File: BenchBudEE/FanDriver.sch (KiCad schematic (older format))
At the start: 10 parts

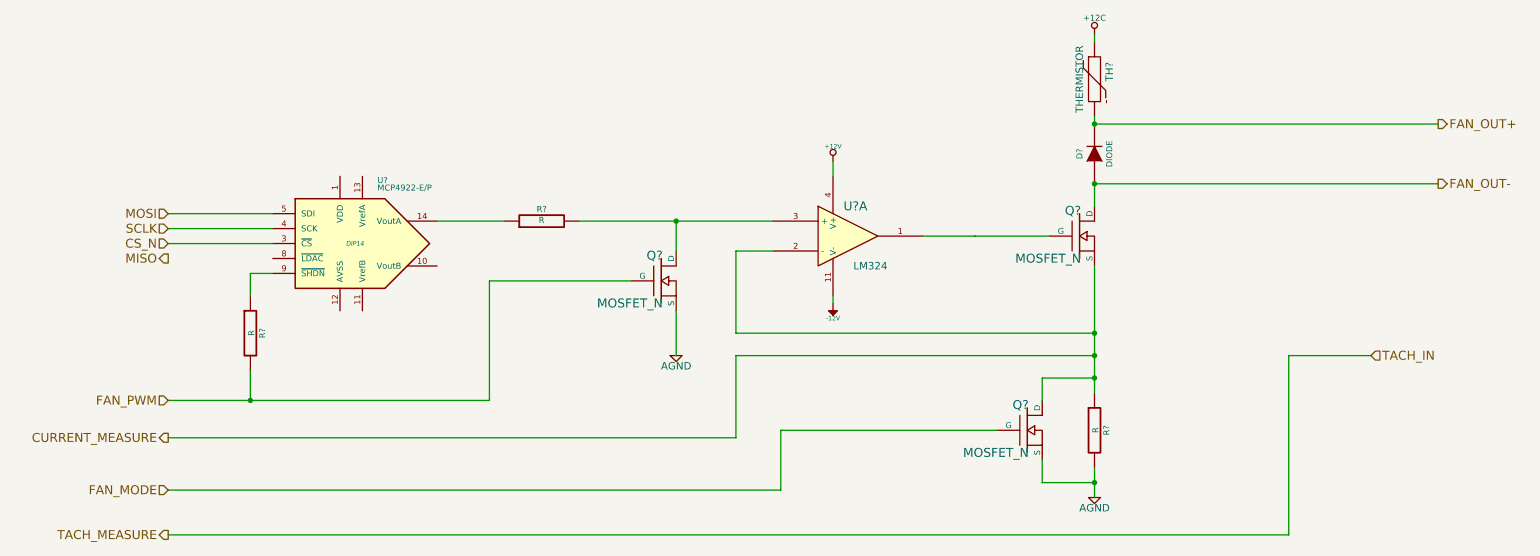
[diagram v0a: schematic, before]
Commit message: Design rules specified for layout.
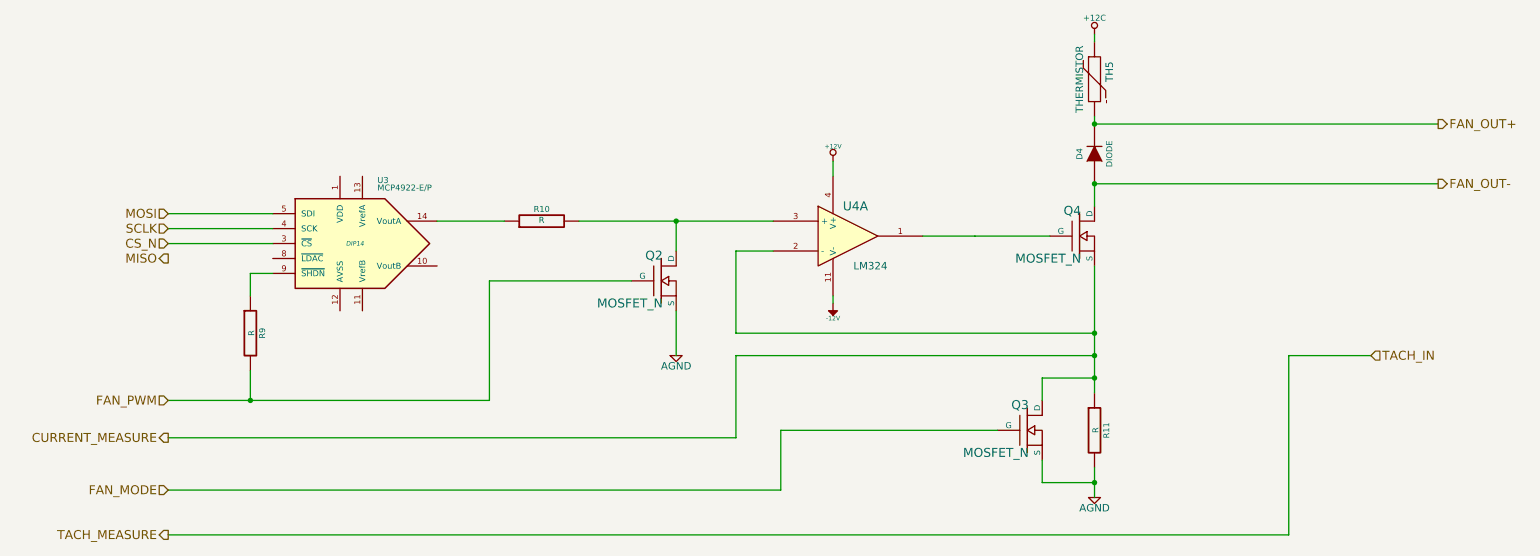
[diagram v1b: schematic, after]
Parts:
- gave numbers to parts that had none: 10
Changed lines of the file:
@@
 FAN_PWM
 $Comp
-L LM324 U?
+L LM324 U4
 U 1 1 52F28A08
 P 6150 2050
-F 0 "U?" H 6200 2250 60  0000 C CNN
+F 0 "U4" H 6200 2250 60  0000 C CNN
 F 1 "LM324" H 6300 1850 50  0000 C CNN
 F 2 "" H 6150 2050 60  0000 C CNN
@@
 $EndComp
 $Comp
-L MOSFET_N Q?
+L MOSFET_N Q4
 U 1 1 52F28A2A
 P 7700 2050
-F 0 "Q?" H 7710 2220 60  0000 R CNN
+F 0 "Q4" H 7710 2220 60  0000 R CNN
 F 1 "MOSFET_N" H 7710 1900 60  0000 R CNN
 F 2 "~" H 7700 2050 60  0000 C CNN
@@
 $EndComp
 $Comp
-L +12V #PWR?
+L +12V #PWR24
 U 1 1 52F28A39
 P 6050 1550
-F 0 "#PWR?" H 6050 1500 20  0001 C CNN
+F 0 "#PWR24" H 6050 1500 20  0001 C CNN
 F 1 "+12V" H 6050 1650 30  0000 C CNN
 F 2 "" H 6050 1550 60  0000 C CNN
@@
 $EndComp
 $Comp
-L R R?
+L R R11
 U 1 1 52F28A75
 P 7800 3350
-F 0 "R?" V 7880 3350 40  0000 C CNN
+F 0 "R11" V 7880 3350 40  0000 C CNN
 F 1 "R" V 7807 3351 40  0000 C CNN
 F 2 "~" V 7730 3350 30  0000 C CNN
@@
 $EndComp
 $Comp
-L AGND #PWR?
+L AGND #PWR27
 U 1 1 52F28A84
 P 7800 3800
-F 0 "#PWR?" H 7800 3800 40  0001 C CNN
+F 0 "#PWR27" H 7800 3800 40  0001 C CNN
 F 1 "AGND" H 7800 3730 50  0000 C CNN
 F 2 "" H 7800 3800 60  0000 C CNN
@@
 $EndComp
 $Comp
-L -12V #PWR?
+L -12V #PWR25
 U 1 1 52F28AAC
 P 6050 2500
-F 0 "#PWR?" H 6050 2630 20  0001 C CNN
+F 0 "#PWR25" H 6050 2630 20  0001 C CNN
 F 1 "-12V" H 6050 2600 30  0000 C CNN
 F 2 "" H 6050 2500 60  0000 C CNN
@@
 $EndComp
 $Comp
-L AGND #PWR?
+L AGND #PWR23
 U 1 1 52F28AF3
 P 5000 2850
-F 0 "#PWR?" H 5000 2850 40  0001 C CNN
+F 0 "#PWR23" H 5000 2850 40  0001 C CNN
 F 1 "AGND" H 5000 2780 50  0000 C CNN
 F 2 "" H 5000 2850 60  0000 C CNN
@@
 $EndComp
 $Comp
-L MCP4922-E/P U?
+L MCP4922-E/P U3
 U 1 1 52F28B29
 P 2850 2100
-F 0 "U?" H 3000 2500 40  0000 L BNN
+F 0 "U3" H 3000 2500 40  0000 L BNN
 F 1 "MCP4922-E/P" H 3000 2450 40  0000 L BNN
 F 2 "DIP14" H 2850 2100 30  0000 C CIN
@@
 CURRENT_MEASURE
 $Comp
-L R R?
+L R R10
 U 1 1 52F28BC3
 P 4100 1950
-F 0 "R?" V 4180 1950 40  0000 C CNN
+F 0 "R10" V 4180 1950 40  0000 C CNN
 F 1 "R" V 4107 1951 40  0000 C CNN
 F 2 "~" V 4030 1950 30  0000 C CNN
@@
 CS_N
 $Comp
-L R R?
+L R R9
 U 1 1 52F28C60
 P 2150 2700
-F 0 "R?" V 2230 2700 40  0000 C CNN
+F 0 "R9" V 2230 2700 40  0000 C CNN
 F 1 "R" V 2157 2701 40  0000 C CNN
 F 2 "~" V 2080 2700 30  0000 C CNN
@@
 $EndComp
 $Comp
-L MOSFET_N Q?
+L MOSFET_N Q3
 U 1 1 52F7E547
 P 7350 3350
-F 0 "Q?" H 7360 3520 60  0000 R CNN
+F 0 "Q3" H 7360 3520 60  0000 R CNN
 F 1 "MOSFET_N" H 7360 3200 60  0000 R CNN
 F 2 "~" H 7350 3350 60  0000 C CNN
@@
 $EndComp
 $Comp
-L THERMISTOR TH?
+L THERMISTOR TH5
 U 1 1 52F7E559
 P 7800 1000
-F 0 "TH?" V 7900 1050 50  0000 C CNN
+F 0 "TH5" V 7900 1050 50  0000 C CNN
 F 1 "THERMISTOR" V 7700 1000 50  0000 C CNN
 F 2 "~" H 7800 1000 60  0000 C CNN
@@
 $EndComp
 $Comp
-L DIODE D?
+L DIODE D4
 U 1 1 52F7E659
 P 7800 1500
-F 0 "D?" H 7800 1600 40  0000 C CNN
+F 0 "D4" H 7800 1600 40  0000 C CNN
 F 1 "DIODE" H 7800 1400 40  0000 C CNN
 F 2 "~" H 7800 1500 60  0000 C CNN
@@
 	9100 2850 9650 2850
 $Comp
-L MOSFET_N Q?
+L MOSFET_N Q2
 U 1 1 52F7E89F
 P 4900 2350
-F 0 "Q?" H 4910 2520 60  0000 R CNN
+F 0 "Q2" H 4910 2520 60  0000 R CNN
 F 1 "MOSFET_N" H 4910 2200 60  0000 R CNN
 F 2 "~" H 4900 2350 60  0000 C CNN
@@
 FAN_MODE
 $Comp
-L +12C #PWR?
+L +12C #PWR26
 U 1 1 52F7ED72
 P 7800 700
-F 0 "#PWR?" H 7800 670 30  0001 C CNN
+F 0 "#PWR26" H 7800 670 30  0001 C CNN
 F 1 "+12C" H 7800 810 40  0000 C CNN
 F 2 "" H 7800 700 60  0000 C CNN
